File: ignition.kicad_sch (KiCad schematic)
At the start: 19 parts, among them J2 Centroid, J4 PYRO1, Q1 PMOS-GSD, Q2 Q_NMOS_GSD, Q3 Q_NMOS_GSD, Q4 Q_NMOS_GSD, U4 CPC1135N

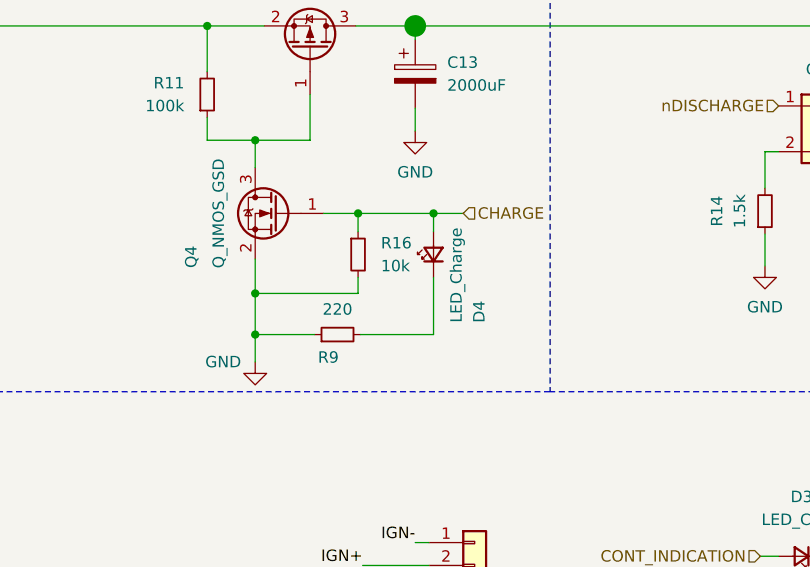
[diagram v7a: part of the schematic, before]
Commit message: #6 Add basic reverse polarity protection
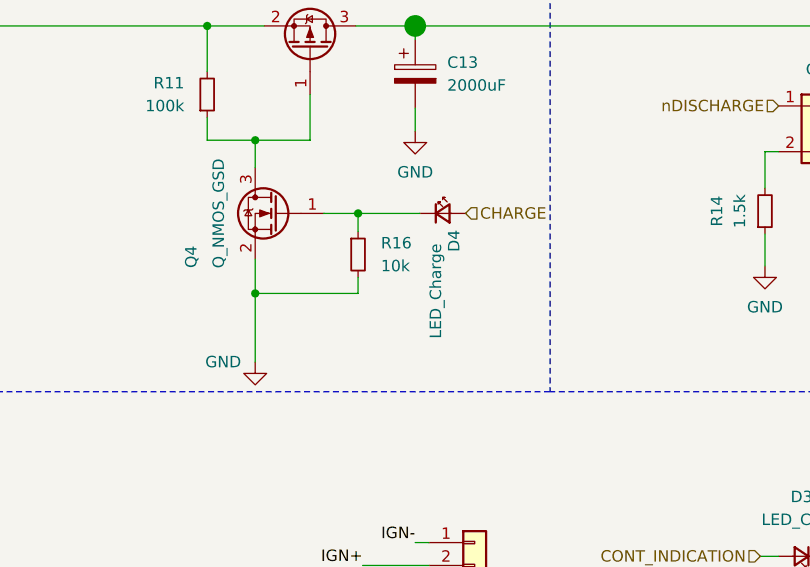
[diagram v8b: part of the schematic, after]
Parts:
- removed R9: 220, Resistor_SMD:R_0402_1005Metric, symbol Device:R_Small
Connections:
- net CHARGE: no longer Q4.1 (G), R16.1
- net at D4.1 (K): now also Q4.1 (G), R16.1
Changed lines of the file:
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@@
   (junction (at 104.394 65.532) (diameter 0.9144) (color 0 0 0 0))
   (junction (at 104.394 82.55) (diameter 0.9144) (color 0 0 0 0))
-  (junction (at 104.394 87.122) (diameter 0.9144) (color 0 0 0 0))
   (junction (at 115.824 73.66) (diameter 0.9144) (color 0 0 0 0))
   (junction (at 122.174 52.832) (diameter 2.4136) (color 0 0 0 0))
-  (junction (at 124.206 73.66) (diameter 0.9144) (color 0 0 0 0))
   (junction (at 179.832 52.832) (diameter 0.9144) (color 0 0 0 0))
   (junction (at 231.394 52.832) (diameter 0.9144) (color 0 0 0 0))
@@
     (stroke (width 0) (type solid) (color 0 0 0 0))
   )
-  (wire (pts (xy 104.394 82.55) (xy 104.394 87.122))
+  (wire (pts (xy 104.394 82.55) (xy 104.394 90.17))
     (stroke (width 0) (type solid) (color 0 0 0 0))
   )
@@
     (stroke (width 0) (type solid) (color 0 0 0 0))
   )
-  (wire (pts (xy 104.394 87.122) (xy 104.394 90.17))
-    (stroke (width 0) (type solid) (color 0 0 0 0))
-  )
   (wire (pts (xy 110.49 60.452) (xy 110.49 65.532))
     (stroke (width 0) (type solid) (color 0 0 0 0))
   )
-  (wire (pts (xy 110.998 87.122) (xy 104.394 87.122))
-    (stroke (width 0) (type solid) (color 0 0 0 0))
-  )
   (wire (pts (xy 112.014 73.66) (xy 115.824 73.66))
     (stroke (width 0) (type solid) (color 0 0 0 0))
@@
     (stroke (width 0) (type solid) (color 0 0 0 0))
   )
-  (wire (pts (xy 115.824 73.66) (xy 124.206 73.66))
+  (wire (pts (xy 115.824 73.66) (xy 122.682 73.66))
     (stroke (width 0) (type solid) (color 0 0 0 0))
   )
@@
     (stroke (width 0) (type solid) (color 0 0 0 0))
   )
-  (wire (pts (xy 116.078 87.122) (xy 124.206 87.122))
-    (stroke (width 0) (type solid) (color 0 0 0 0))
-  )
   (wire (pts (xy 116.332 112.776) (xy 123.698 112.776))
     (stroke (width 0) (type solid) (color 0 0 0 0))
@@
   )
   (wire (pts (xy 122.174 110.236) (xy 123.698 110.236))
-    (stroke (width 0) (type solid) (color 0 0 0 0))
-  )
-  (wire (pts (xy 124.206 73.66) (xy 124.206 75.692))
-    (stroke (width 0) (type solid) (color 0 0 0 0))
-  )
-  (wire (pts (xy 124.206 73.66) (xy 127.508 73.66))
-    (stroke (width 0) (type solid) (color 0 0 0 0))
-  )
-  (wire (pts (xy 124.206 87.122) (xy 124.206 80.772))
     (stroke (width 0) (type solid) (color 0 0 0 0))
   )
@@
     (effects (font (size 1.27 1.27)) (justify right))
   )
-  (hierarchical_label "CHARGE" (shape input) (at 127.508 73.66 0)
+  (hierarchical_label "CHARGE" (shape input) (at 127.762 73.66 0)
     (effects (font (size 1.27 1.27)) (justify left))
   )
@@
     (pin "2")
   )
-  (symbol (lib_id "Device:R_Small") (at 113.538 87.122 90) (unit 1)
-    (in_bom yes) (on_board yes)
-    (property "Reference" "R9" (id 0) (at 112.522 89.662 90))
-    (property "Value" "220" (id 1) (at 113.538 84.328 90))
-    (property "Footprint" "Resistor_SMD:R_0402_1005Metric" (id 2) (at 113.538 87.122 0)
-      (effects (font (size 1.27 1.27)) hide)
-    )
-    (property "Datasheet" "~" (id 3) (at 113.538 87.122 0)
-      (effects (font (size 1.27 1.27)) hide)
-    )
-    (pin "1")
-    (pin "2")
-  )
   (symbol (lib_id "Device:R_Small") (at 115.824 78.232 0) (unit 1)
     (in_bom yes) (on_board yes) (fields_autoplaced)
@@
     (pin "2")
   )
-  (symbol (lib_id "Device:LED_Small") (at 124.206 78.232 90) (unit 1)
+  (symbol (lib_id "Device:LED_Small") (at 125.222 73.66 0) (unit 1)
     (in_bom yes) (on_board yes)
-    (property "Reference" "D4" (id 0) (at 129.286 84.582 0))
-    (property "Value" "LED_Charge" (id 1) (at 126.746 80.518 0))
-    (property "Footprint" "LED_SMD:LED_0603_1608Metric" (id 2) (at 124.206 78.232 90)
-      (effects (font (size 1.27 1.27)) hide)
-    )
-    (property "Datasheet" "~" (id 3) (at 124.206 78.232 90)
-      (effects (font (size 1.27 1.27)) hide)
-    )
+    (property "Reference" "D4" (id 0) (at 126.492 76.708 90))
+    (property "Value" "LED_Charge" (id 1) (at 124.46 82.296 90))
+    (property "Footprint" "LED_SMD:LED_0603_1608Metric" (id 2) (at 125.222 73.66 90)
+      (effects (font (size 1.27 1.27)) hide)
+    )
+    (property "Datasheet" "~" (id 3) (at 125.222 73.66 90)
+      (effects (font (size 1.27 1.27)) hide)
+    )
